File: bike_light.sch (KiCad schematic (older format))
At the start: 20 parts

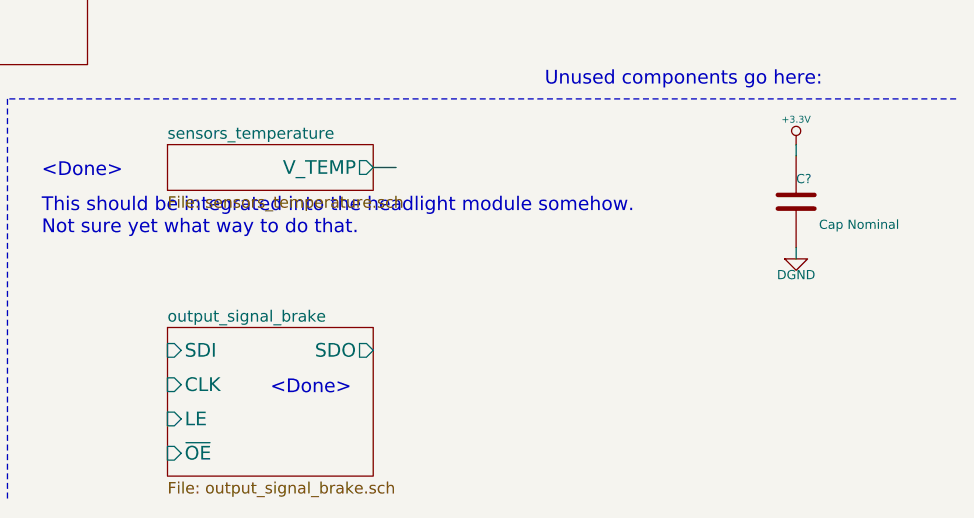
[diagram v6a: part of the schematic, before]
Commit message: various fixes due to issues found in ERC
learned how to use invisible pins
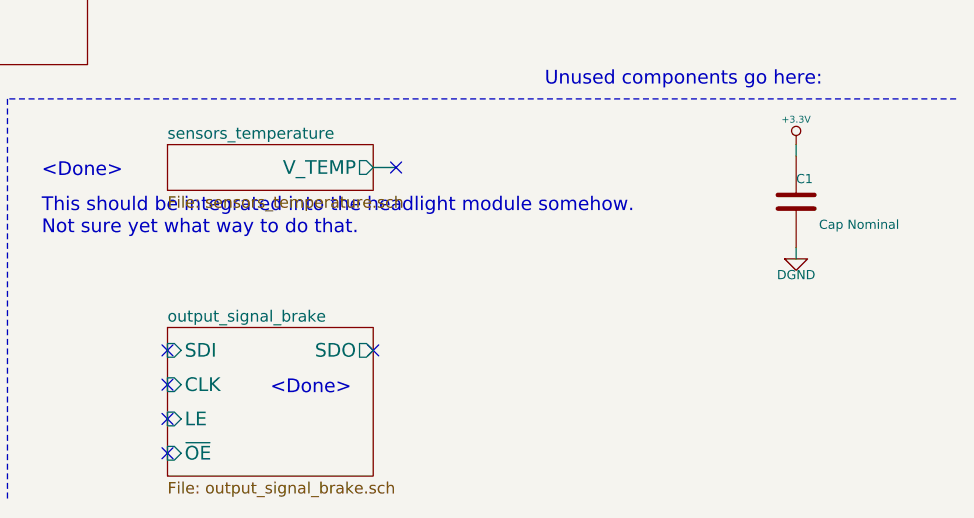
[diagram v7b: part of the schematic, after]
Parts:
- gave numbers to parts that had none: 20
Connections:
- no-connect marks 0 -> 6
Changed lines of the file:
@@
 Sheet 1 18
 Title "Bike Light"
-Date "18 dec 2013"
+Date "20 dec 2013"
 Rev "1.0"
 Comp ""
@@
 	5400 3900 5500 3900
 $Comp
-L +3.3V #PWR?
+L +3.3V #PWR01
 U 1 1 52A50B64
 P 3700 1000
-F 0 "#PWR?" H 3700 960 30  0001 C CNN
+F 0 "#PWR01" H 3700 960 30  0001 C CNN
 F 1 "+3.3V" H 3700 1110 30  0000 C CNN
 F 2 "" H 3700 1000 60  0000 C CNN
@@
 $EndSheet
 $Comp
-L C C?
+L C C1
 U 1 1 52A6923B
 P 9800 6050
-F 0 "C?" H 9800 6150 40  0000 L CNN
+F 0 "C1" H 9800 6150 40  0000 L CNN
 F 1 "Cap Nominal" H 9900 5950 40  0000 L CNN
 F 2 "~" H 9838 5900 30  0000 C CNN
@@
 $EndComp
 $Comp
-L +3.3V #PWR?
+L +3.3V #PWR02
 U 1 1 52A69241
 P 9800 5800
-F 0 "#PWR?" H 9800 5760 30  0001 C CNN
+F 0 "#PWR02" H 9800 5760 30  0001 C CNN
 F 1 "+3.3V" H 9800 5910 30  0000 C CNN
 F 2 "" H 9800 5800 60  0000 C CNN
@@
 $EndComp
 $Comp
-L DGND #PWR?
+L DGND #PWR03
 U 1 1 52A69247
 P 9800 6300
-F 0 "#PWR?" H 9800 6300 40  0001 C CNN
+F 0 "#PWR03" H 9800 6300 40  0001 C CNN
 F 1 "DGND" H 9800 6230 40  0000 C CNN
 F 2 "" H 9800 6300 60  0000 C CNN
@@
 $EndSheet
 $Comp
-L TEST_PT U?
+L TEST_PT U6
 U 1 1 52B19189
 P 6850 1800
-F 0 "U?" H 6850 1600 60  0001 C CNN
+F 0 "U6" H 6850 1600 60  0001 C CNN
 F 1 "TEST_PT" H 6850 2000 60  0001 C CNN
 F 2 "~" H 6850 1800 60  0000 C CNN
@@
 $EndComp
 $Comp
-L TEST_PT U?
+L TEST_PT U5
 U 1 1 52B1A44A
 P 8050 1650
-F 0 "U?" H 8050 1450 60  0001 C CNN
+F 0 "U5" H 8050 1450 60  0001 C CNN
 F 1 "TEST_PT" H 8050 1850 60  0001 C CNN
 F 2 "~" H 8050 1650 60  0000 C CNN
@@
 	6950 1800 7000 1800
 $Comp
-L TEST_PT U?
+L TEST_PT U1
 U 1 1 52B1ED13
 P 9400 1150
-F 0 "U?" H 9400 950 60  0001 C CNN
+F 0 "U1" H 9400 950 60  0001 C CNN
 F 1 "TEST_PT" H 9400 1350 60  0001 C CNN
 F 2 "~" H 9400 1150 60  0000 C CNN
@@
 $EndComp
 $Comp
-L TEST_PT U?
+L TEST_PT U2
 U 1 1 52B1ED19
 P 9400 1400
-F 0 "U?" H 9400 1200 60  0001 C CNN
+F 0 "U2" H 9400 1200 60  0001 C CNN
 F 1 "TEST_PT" H 9400 1600 60  0001 C CNN
 F 2 "~" H 9400 1400 60  0000 C CNN
@@
 $EndComp
 $Comp
-L TEST_PT U?
+L TEST_PT U4
 U 1 1 52B1ED1F
 P 9400 1550
-F 0 "U?" H 9400 1350 60  0001 C CNN
+F 0 "U4" H 9400 1350 60  0001 C CNN
 F 1 "TEST_PT" H 9400 1750 60  0001 C CNN
 F 2 "~" H 9400 1550 60  0000 C CNN
@@
 $EndComp
 $Comp
-L TEST_PT U?
+L TEST_PT U15
 U 1 1 52B2155E
 P 4350 4100
-F 0 "U?" H 4350 3900 60  0001 C CNN
+F 0 "U15" H 4350 3900 60  0001 C CNN
 F 1 "TEST_PT" H 4350 4300 60  0001 C CNN
 F 2 "~" H 4350 4100 60  0000 C CNN
@@
 	4450 4100 4500 4100
 $Comp
-L TEST_PT U?
+L TEST_PT U19
 U 1 1 52B2295F
 P 4350 4750
-F 0 "U?" H 4350 4550 60  0001 C CNN
+F 0 "U19" H 4350 4550 60  0001 C CNN
 F 1 "TEST_PT" H 4350 4950 60  0001 C CNN
 F 2 "~" H 4350 4750 60  0000 C CNN
@@
 Connection ~ 2450 1150
 $Comp
-L TEST_PT U?
+L TEST_PT U7
 U 1 1 52B2B981
 P 1000 2250
-F 0 "U?" H 1000 2050 60  0001 C CNN
+F 0 "U7" H 1000 2050 60  0001 C CNN
 F 1 "TEST_PT" H 1000 2450 60  0001 C CNN
 F 2 "~" H 1000 2250 60  0000 C CNN
@@
 $EndComp
 $Comp
-L TEST_PT U?
+L TEST_PT U3
 U 1 1 52B2C8DE
 P 3750 1450
-F 0 "U?" H 3750 1250 60  0001 C CNN
+F 0 "U3" H 3750 1250 60  0001 C CNN
 F 1 "TEST_PT" H 3750 1650 60  0001 C CNN
 F 2 "~" H 3750 1450 60  0000 C CNN
@@
 Connection ~ 3750 1300
 $Comp
-L TEST_PT U?
+L TEST_PT U12
 U 1 1 52B32F47
 P 5450 3600
-F 0 "U?" H 5450 3400 60  0001 C CNN
+F 0 "U12" H 5450 3400 60  0001 C CNN
 F 1 "TEST_PT" H 5450 3800 60  0001 C CNN
 F 2 "~" H 5450 3600 60  0000 C CNN
@@
 $EndComp
 $Comp
-L TEST_PT U?
+L TEST_PT U14
 U 1 1 52B3393A
 P 5450 4050
-F 0 "U?" H 5450 3850 60  0001 C CNN
+F 0 "U14" H 5450 3850 60  0001 C CNN
 F 1 "TEST_PT" H 5450 4250 60  0001 C CNN
 F 2 "~" H 5450 4050 60  0000 C CNN
@@
 Connection ~ 5450 3900
 $Comp
-L TEST_PT U?
+L TEST_PT U18
 U 1 1 52B350A4
 P 4050 4150
-F 0 "U?" H 4050 3950 60  0001 C CNN
+F 0 "U18" H 4050 3950 60  0001 C CNN
 F 1 "TEST_PT" H 4050 4350 60  0001 C CNN
 F 2 "~" H 4050 4150 60  0000 C CNN
@@
 $EndComp
 $Comp
-L TEST_PT U?
+L TEST_PT U17
 U 1 1 52B350AA
 P 3900 4150
-F 0 "U?" H 3900 3950 60  0001 C CNN
+F 0 "U17" H 3900 3950 60  0001 C CNN
 F 1 "TEST_PT" H 3900 4350 60  0001 C CNN
 F 2 "~" H 3900 4150 60  0000 C CNN
@@
 $EndComp
 $Comp
-L TEST_PT U?
+L TEST_PT U16
 U 1 1 52B350B0
 P 3750 4150
-F 0 "U?" H 3750 3950 60  0001 C CNN
+F 0 "U16" H 3750 3950 60  0001 C CNN
 F 1 "TEST_PT" H 3750 4350 60  0001 C CNN
 F 2 "~" H 3750 4150 60  0000 C CNN
@@
 Connection ~ 3750 4600
 $Comp
-L TEST_PT U?
+L TEST_PT U11
 U 1 1 52B35EA5
 P 5450 3350
-F 0 "U?" H 5450 3150 60  0001 C CNN
+F 0 "U11" H 5450 3150 60  0001 C CNN
 F 1 "TEST_PT" H 5450 3550 60  0001 C CNN
 F 2 "~" H 5450 3350 60  0000 C CNN
@@
 Connection ~ 5450 3200
 $Comp
-L TEST_PT U?
+L TEST_PT U8
 U 1 1 52B38585
 P 2350 2800
-F 0 "U?" H 2350 2600 60  0001 C CNN
+F 0 "U8" H 2350 2600 60  0001 C CNN
 F 1 "TEST_PT" H 2350 3000 60  0001 C CNN
 F 2 "~" H 2350 2800 60  0000 C CNN
@@
 	2900 2950 2200 2950
 $Comp
-L TEST_PT U?
+L TEST_PT U9
 U 1 1 52B3BE57
 P 2350 3150
-F 0 "U?" H 2350 2950 60  0001 C CNN
+F 0 "U9" H 2350 2950 60  0001 C CNN
 F 1 "TEST_PT" H 2350 3350 60  0001 C CNN
 F 2 "~" H 2350 3150 60  0000 C CNN
@@
 $EndComp
 $Comp
-L TEST_PT U?
+L TEST_PT U10
 U 1 1 52B3C205
 P 2350 3300
-F 0 "U?" H 2350 3100 60  0001 C CNN
+F 0 "U10" H 2350 3100 60  0001 C CNN
 F 1 "TEST_PT" H 2350 3500 60  0001 C CNN
 F 2 "~" H 2350 3300 60  0000 C CNN
@@
 	2250 3300 2200 3300
 $Comp
-L TEST_PT U?
+L TEST_PT U13
 U 1 1 52B3F6D1
 P 4350 3750
-F 0 "U?" H 4350 3550 60  0001 C CNN
+F 0 "U13" H 4350 3550 60  0001 C CNN
 F 1 "TEST_PT" H 4350 3950 60  0001 C CNN
 F 2 "~" H 4350 3750 60  0000 C CNN
@@
 Wire Wire Line
 	4450 3750 4500 3750
+NoConn ~ 8050 5900
+NoConn ~ 7050 6700
+NoConn ~ 7050 6850
+NoConn ~ 7050 7000
+NoConn ~ 7050 7150
+NoConn ~ 7950 6700
 $EndSCHEMATC
